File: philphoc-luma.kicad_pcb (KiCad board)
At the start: 2 copper layers, 62.5 x 47 mm, 49 parts, among them J1 SWD, J10 M3, J2 E75_proc, J3 USB_C, J4 OUT, J5 IN, J6 I2C, J7 M3, J8 M3, J9 M3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

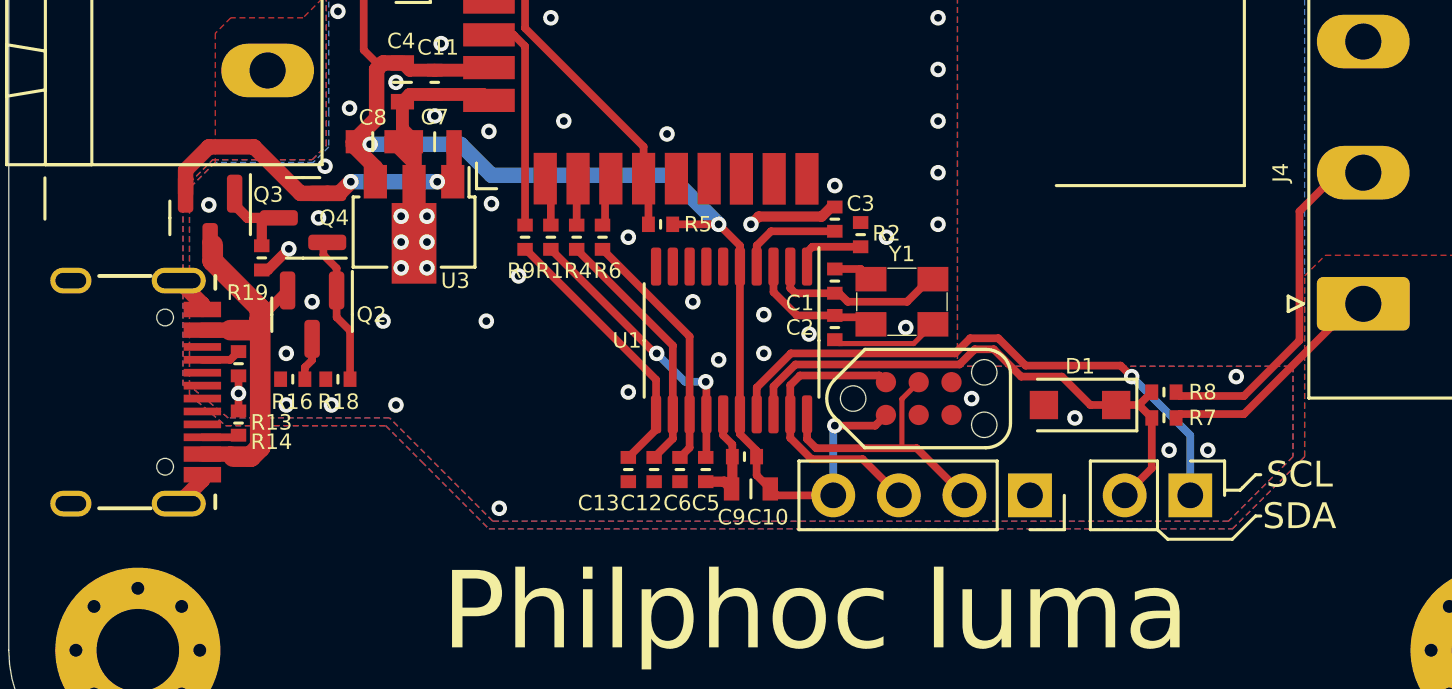
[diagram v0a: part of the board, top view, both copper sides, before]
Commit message: exchanged STM32f030 for STM32G030
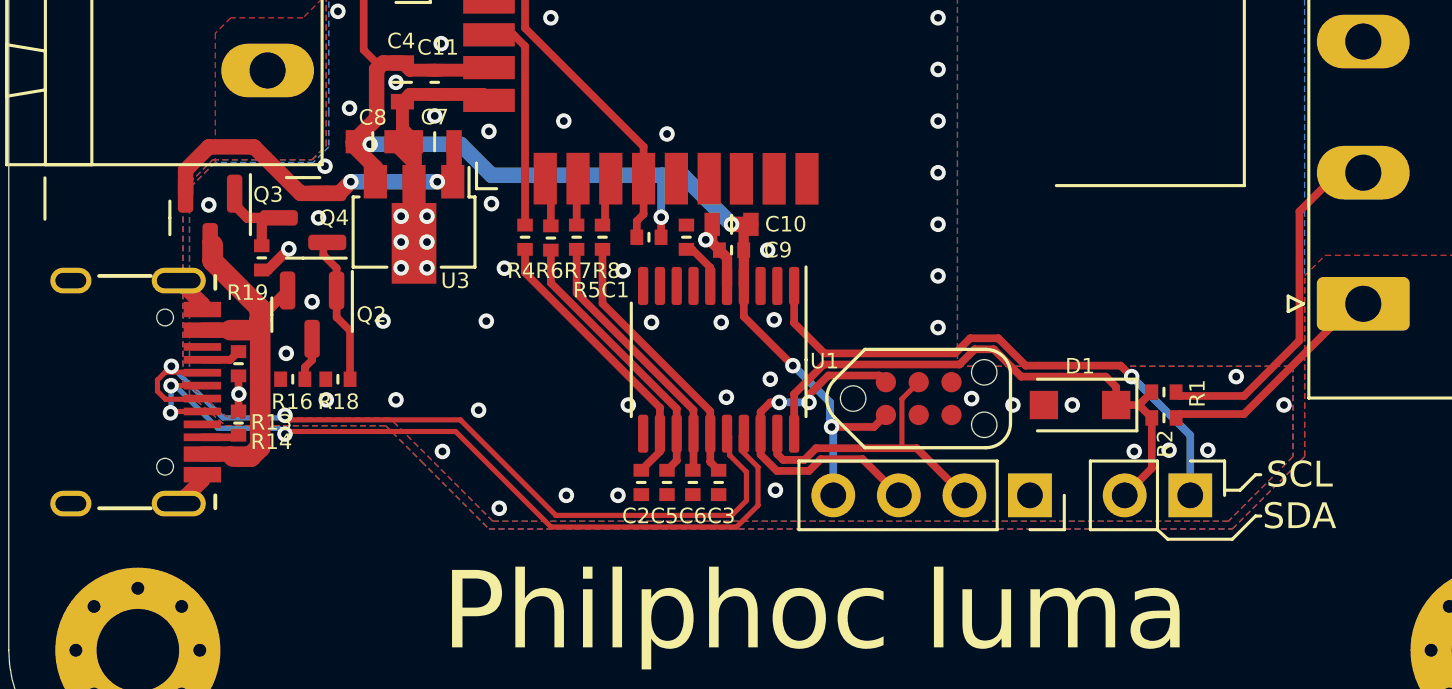
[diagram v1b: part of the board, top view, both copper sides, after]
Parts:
- removed C12, C13: 100n, otter:C_0402
- removed R9: 100k, otter:R_0402
- removed Y1: 8Mhz, otter:Oscillator_3225
- C1, C2: value 18p -> 100n
- J1: value SWD -> OUT; footprint otter:PinSocket_1x04_P2.54mm_Vertical_center -> Connector_Phoenix_MSTB:PhoenixContact_MSTBA_2,5_3-G-5,08_1x03_P5.08mm_Horizontal
- J4: value OUT -> I2C; footprint Connector_Phoenix_MSTB:PhoenixContact_MSTBA_2,5_3-G-5,08_1x03_P5.08mm_Horizontal -> otter:PinHeader_1x02_P2.54mm_Vertical
- J6: value I2C -> SWD; footprint otter:PinHeader_1x02_P2.54mm_Vertical -> otter:PinSocket_1x04_P2.54mm_Vertical_center
- R1: value 100k -> 20
- R7: value 5k1 -> 100k
- R8: value 20 -> 100k
- U1: value STM32F030F4Px -> STM32G030F6P6
- moved R1 24.5 mm to (94.8, 83.5), turned to 180 degrees
- moved R7 23.8 mm to (72.0, 77.5), turned to 90 degrees
- moved R8 22.6 mm to (73.0, 77.5), turned to 90 degrees
- moved J1 18.3 mm to (102.5, 80.1), turned to 90 degrees
- moved R2 13.7 mm to (94.8, 84.5), turned to 0 degrees
- moved C3 11.1 mm to (77.5, 87.0), turned to -90 degrees
- moved J4 10.9 mm to (94.5, 87.5), turned to -90 degrees
- moved C10 10.3 mm to (78.0, 77.0)
- moved C2 9.60 mm to (74.5, 87.0)
- moved J6 8.75 mm to (85.8, 87.5)
- moved C9 8.02 mm to (78.0, 78.0)
- moved C1 6.00 mm to (76.2, 77.5)
- moved R6 2.00 mm to (71.0, 77.5)
- moved R4 2.00 mm to (70.0, 77.5)
- moved C5 1.58 mm to (75.5, 87.0)
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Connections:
- J1 pad 1: GND -> VBUS
- J1 pad 2: SWCLK -> Net-(J1-Pad2)
- J1 pad 3: SWDIO -> GND
- J3 pad A6: unconnected-(J3-PadA6) -> D+
- J3 pad A7: unconnected-(J3-PadA7) -> D-
- J3 pad B6: unconnected-(J3-PadB6) -> D+
- J3 pad B7: unconnected-(J3-PadB7) -> D-
- J4 pad 1: VBUS -> Net-(J4-Pad1)
- J4 pad 2: Net-(J4-Pad2) -> Net-(D1-Pad1)
- J6 pad 1: Net-(J6-Pad1) -> GND
- J6 pad 2: Net-(D1-Pad1) -> SWCLK
- R1 pad 1: Net-(C5-Pad1) -> Net-(J1-Pad2)
- R1 pad 2: PWM_R -> Net-(D1-Pad1)
- R2 pad 1: Net-(R2-Pad1) -> Net-(D1-Pad1)
- R2 pad 2: GND -> VBUS
- R4 pad 1: Net-(C12-Pad1) -> Net-(C2-Pad1)
- R4 pad 2: PWM_G -> PWM_1
- R6 pad 1: Net-(C6-Pad1) -> Net-(C5-Pad1)
- R6 pad 2: PWM_B -> PWM_R
- R7 pad 1: Net-(D1-Pad1) -> Net-(C6-Pad1)
- R7 pad 2: VBUS -> PWM_G
- R8 pad 1: Net-(J4-Pad2) -> Net-(C3-Pad1)
- R8 pad 2: Net-(D1-Pad1) -> PWM_B
- U1 pad 1: Net-(R2-Pad1) -> Net-(J4-Pad1)
- U1 pad 11: Net-(U1-Pad11) -> unconnected-(U1-Pad11)
- U1 pad 12: Net-(C12-Pad1) -> Net-(C2-Pad1)
- U1 pad 13: Net-(C6-Pad1) -> Net-(C5-Pad1)
- U1 pad 14: Net-(C5-Pad1) -> Net-(C6-Pad1)
- U1 pad 15: GND -> Net-(C3-Pad1)
- U1 pad 16: +3V3 -> D-
- U1 pad 17: Net-(J6-Pad1) -> D+
- U1 pad 18: Net-(D1-Pad1) -> SWDIO
- U1 pad 19: SWDIO -> SWCLK
- U1 pad 2: Net-(C1-Pad1) -> unconnected-(U1-Pad2)
- U1 pad 20: SWCLK -> Net-(D1-Pad1)
- U1 pad 3: Net-(C2-Pad1) -> unconnected-(U1-Pad3)
- U1 pad 4: Net-(C3-Pad1) -> +3V3
- U1 pad 5: +3V3 -> GND
- U1 pad 6: unconnected-(U1-Pad6) -> Net-(C1-Pad1)
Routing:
- net D-: track 0.00 -> 32.3 mm, vias 0 -> 2
- net D+: track 0.00 -> 32.1 mm, vias 0 -> 3
- net Net-(J6-Pad1): track 22.5 -> 0.00 mm, vias 1 -> 0
- net Net-(J4-Pad1): track 0.00 -> 21.4 mm, vias 0 -> 1
- net Net-(J4-Pad2): track 13.8 -> 0.00 mm
- net Net-(J1-Pad2): track 0.00 -> 13.8 mm
- net GND: track 32.6 -> 21.8 mm, vias 70 -> 77
- net Net-(U1-Pad11): track 10.6 -> 0.00 mm
- net Net-(C12-Pad1): track 9.90 -> 0.00 mm
- net Net-(C3-Pad1): track 4.07 -> 10.4 mm
- net Net-(C2-Pad1): track 5.28 -> 11.0 mm
- net Net-(C1-Pad1): track 6.94 -> 1.93 mm
- net Net-(R2-Pad1): track 2.72 -> 0.00 mm
- net SWDIO: track 11.1 -> 13.8 mm, vias 0 -> 2
- net +3V3: track 63.1 -> 60.8 mm, vias 3 -> 5
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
